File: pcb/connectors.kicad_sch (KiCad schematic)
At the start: 5 parts, among them CN1 STDC14, CN2 SM04B-SRSS-TB (LF)(SN), CN4 SM04B-SRSS-TB (LF)(SN), J1 Conn_01x12, J2 Conn_01x16

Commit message: Work on schematics
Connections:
- net GND: now reaches CN2.1
- net GND: now also CN1.11 (GNDD), CN1.2 (GND), CN1.5 (GND)
- net +3V3: now reaches CN2.2
- net +3V3: now also CN1.3 (VCC)
- net I2C1_SDA: now reaches CN2.3
- net I2C1_SCL: now reaches CN2.4
- net NRST: now reaches CN1.12 (~{RST})
- net UART_RX: now reaches CN1.13 (VCP_RX)
- net UART_TX: now reaches CN1.14 (VCP_TX)
- net SWDIO: now reaches CN1.4 (SWDIO)
- net SWCLK: now reaches CN1.6 (SWCLK)
- no-connect marks 0 -> 7
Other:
- moved on the sheet: CN4

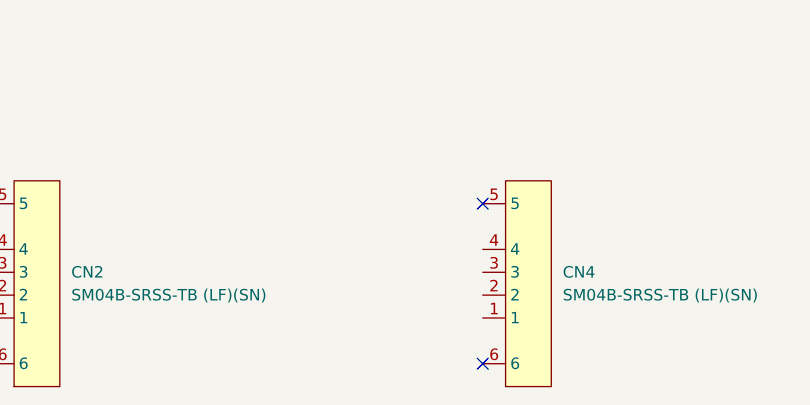
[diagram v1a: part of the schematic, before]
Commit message: Added CubeMX template, and more schematics work
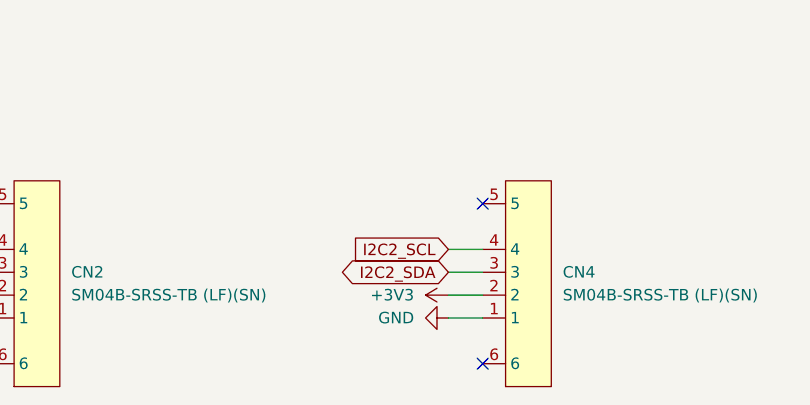
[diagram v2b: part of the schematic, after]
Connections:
- net +3V3: now also CN4.2
- net GND: now also CN4.1
- net I2C2_SDA: now reaches CN4.3
- net I2C2_SCL: now reaches CN4.4

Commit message: Lots of work on schematics
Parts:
- added D4: ESDALC6V1W5, prop-devboard:SOT-323-5_L2.0-W1.3-LS2.1-BL, symbol prop-devboard:ESDALC6V1W5
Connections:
- net +3V3: now also J2.2 (Pin_2), J2.3 (Pin_3)
- net GND: now also J2.4 (Pin_4), D4.2
- net NRST: now also J2.1 (Pin_1)
- net SWCLK: now also D4.4
- net SWDIO: now also D4.5
- net UART_RX: now also J2.14 (Pin_14), D4.1
- net UART_TX: now also J2.15 (Pin_15), D4.3
- net ANALOG5: now reaches J2.10 (Pin_10)
- net SPI_SCK: now reaches J2.11 (Pin_11)
- net SPI_MOSI: now reaches J2.12 (Pin_12)
- net SPI_MISO: now reaches J2.13 (Pin_13)
- net BOOT0: now reaches J2.16 (Pin_16)
- net ANALOG0: now reaches J2.5 (Pin_5)
- net ANALOG1: now reaches J2.6 (Pin_6)
- net ANALOG2: now reaches J2.7 (Pin_7)
- net ANALOG3: now reaches J2.8 (Pin_8)
- net ANALOG4: now reaches J2.9 (Pin_9)
- net VBAT: now reaches J1.1 (Pin_1)
- net DIGITAL5: now reaches J1.10 (Pin_10)
- net I2C3_SCL: now reaches J1.11 (Pin_11)
- net I2C3_SDA: now reaches J1.12 (Pin_12)
- net VREG_EN: now reaches J1.2 (Pin_2)
- net VBUS: now reaches J1.3 (Pin_3)
- net DIGITAL13: now reaches J1.4 (Pin_4)
- net DIGITAL12: now reaches J1.5 (Pin_5)
- net DIGITAL11: now reaches J1.6 (Pin_6)
- net DIGITAL10: now reaches J1.7 (Pin_7)
- net DIGITAL9: now reaches J1.8 (Pin_8)
- net DIGITAL6: now reaches J1.9 (Pin_9)
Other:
- moved on the sheet: CN1, CN2, CN4, J1, J2

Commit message: Mostly finished PCB layout
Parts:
- removed D4: ESDALC6V1W5, prop-devboard:SOT-323-5_L2.0-W1.3-LS2.1-BL, symbol prop-devboard:ESDALC6V1W5

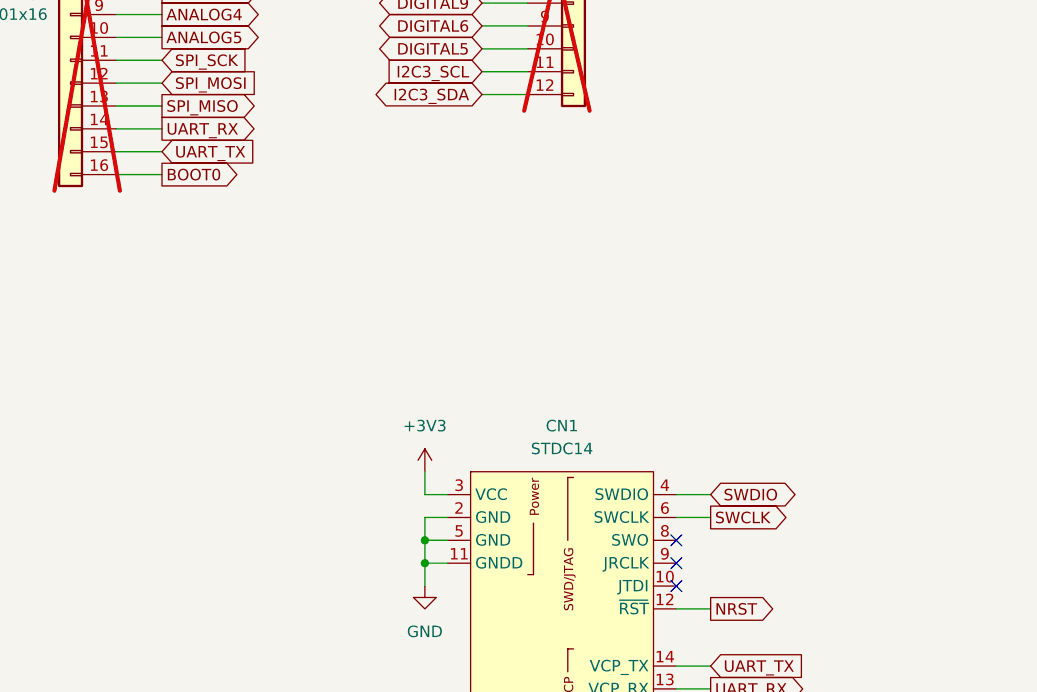
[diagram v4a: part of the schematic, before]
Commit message: Fixed MCU power pins not being connected correctly
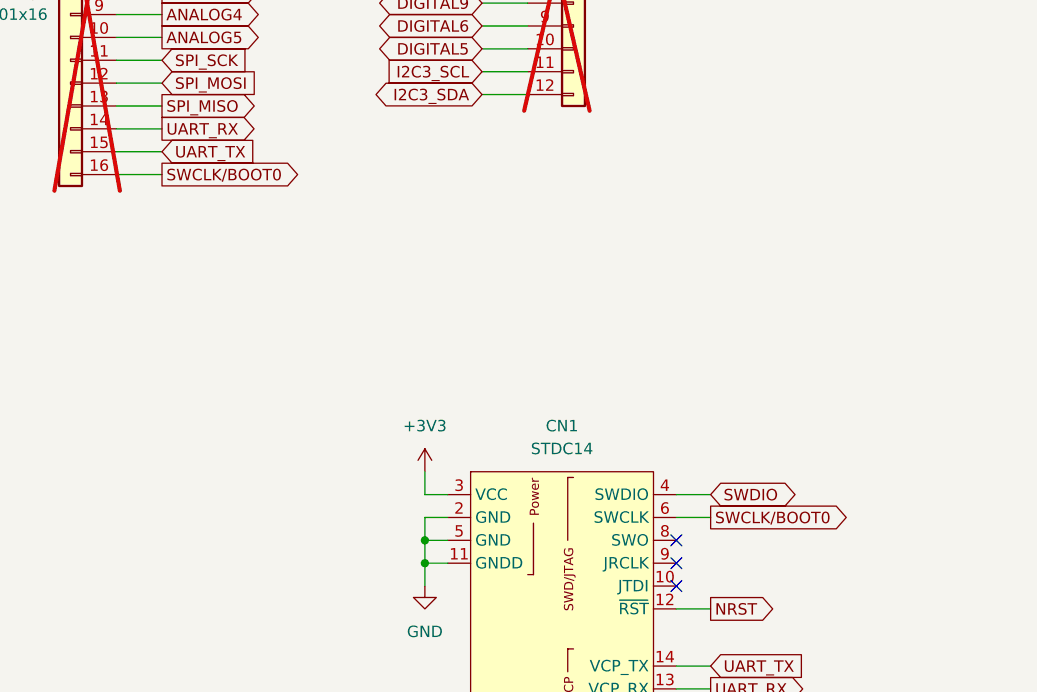
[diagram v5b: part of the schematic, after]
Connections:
- net SWCLK is gone; now on net SWCLK/BOOT0: CN1.6 (SWCLK)
- net BOOT0 renamed SWCLK/BOOT0
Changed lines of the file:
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@@
 		)
 	)
-	(global_label "BOOT0"
+	(global_label "SWCLK{slash}BOOT0"
 		(shape output)
 		(at 44.45 64.77 0)
@@
 		)
 		(property "Intersheetrefs" "${INTERSHEET_REFS}"
-			(at 53.5433 64.77 0)
+			(at 61.1028 64.77 0)
 			(effects
 				(font
@@
 		)
 	)
-	(global_label "SWCLK"
+	(global_label "SWCLK{slash}BOOT0"
 		(shape output)
 		(at 105.41 102.87 0)
@@
 		)
 		(property "Intersheetrefs" "${INTERSHEET_REFS}"
-			(at 114.6242 102.87 0)
+			(at 122.0628 102.87 0)
 			(effects
 				(font

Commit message: Switched battery and QWIIC connectors to black ones, and fixed their positioning to not obstruct bolt heads when M2.5 cylindrical bolts are used to mount the board
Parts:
- CN2, CN4: LCSC Part C160404 -> C19270571
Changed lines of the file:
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@@
 			)
 		)
-		(property "LCSC Part" "C160404"
+		(property "LCSC Part" "C19270571"
 			(at 163.83 38.1 0)
+			(effects
+				(font
+					(size 1.27 1.27)
+				)
+				(hide yes)
+			)
+		)
+		(property "LCSC Part #" ""
+			(at 154.94 38.1 0)
 			(effects
 				(font
@@
 			)
 		)
-		(property "LCSC Part" "C160404"
+		(property "LCSC Part" "C19270571"
 			(at 219.71 38.1 0)
 			(effects
 				(font
+					(size 1.27 1.27)
+				)
+				(hide yes)
+			)
+		)
+		(property "LCSC Part #" ""
+			(at 210.82 38.1 0)
+			(effects
+				(font
